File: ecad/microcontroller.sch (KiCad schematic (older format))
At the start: 2 parts, among them J4 Nucleo_F446_LHS, J5 Nucleo_F446_RHS

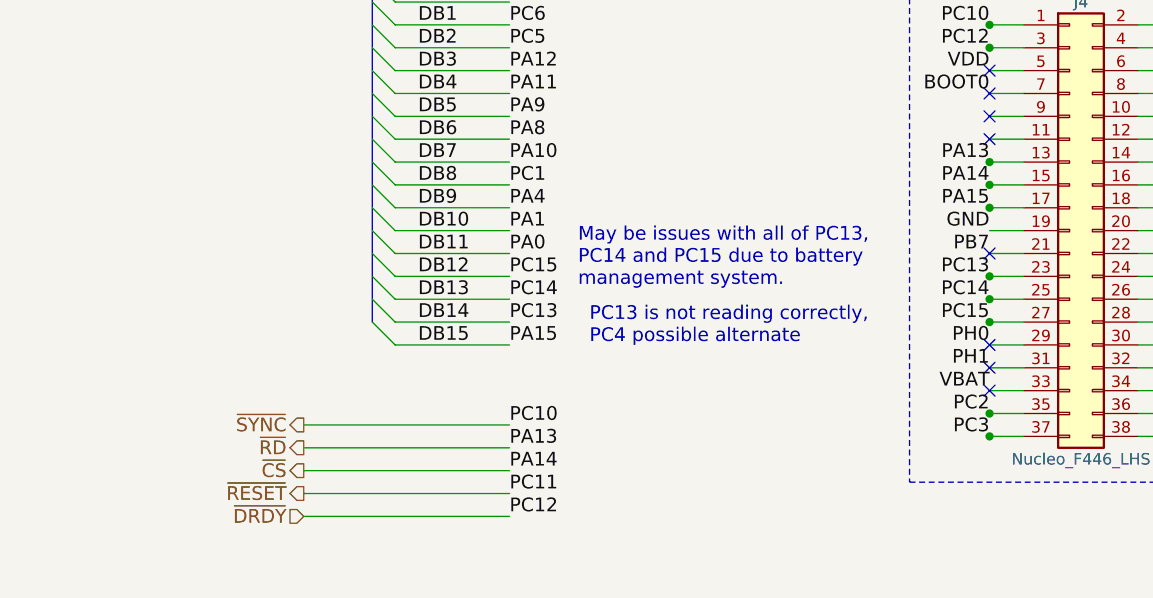
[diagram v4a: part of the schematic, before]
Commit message: Sort out all necessary pin changes.
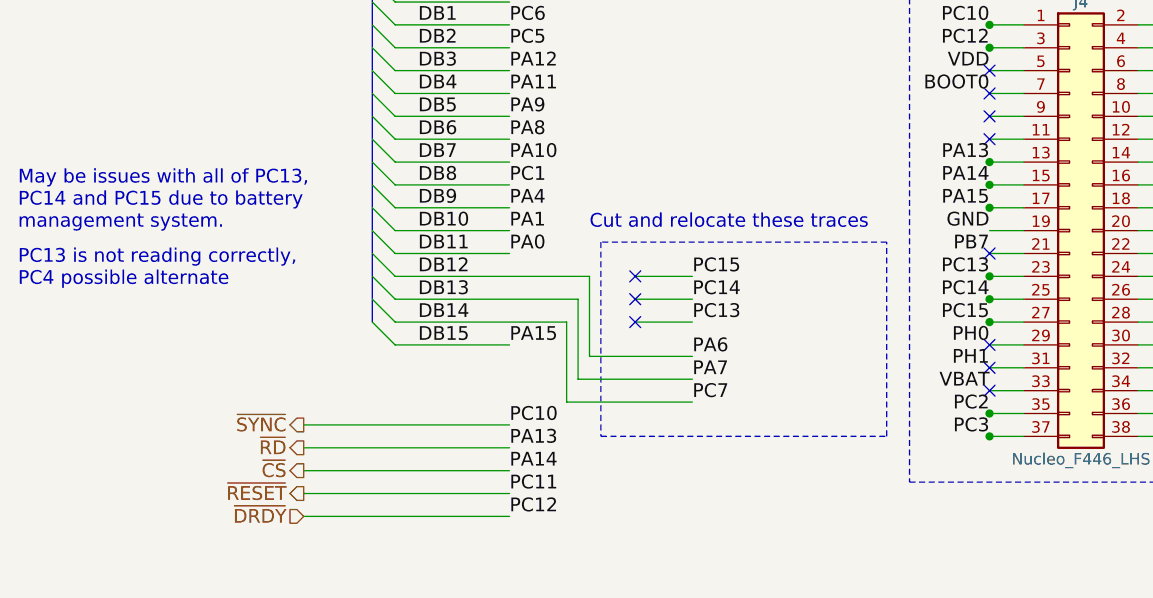
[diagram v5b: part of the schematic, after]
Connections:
- net PA6 is gone; now on net DB12: J5.13 (Pin_13)
- net PA7 is gone; now on net DB13: J5.15 (Pin_15)
- net PC7 is gone; now on net DB14: J5.19 (Pin_19)
- net DB12: no longer J4.27 (Pin_27)
- net DB13: no longer J4.25 (Pin_25)
- net DB14: no longer J4.23 (Pin_23)
- new net PC13: J4.23 (Pin_23)
- new net PC14: J4.25 (Pin_25)
- new net PC15: J4.27 (Pin_27)
- no-connect marks 48 -> 51
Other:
- note added: "Cut and relocate these traces"
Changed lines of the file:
@@
 Text Label 6150 3500 0    60   ~ 0
 PC12
-Text Label 6150 2650 0    60   ~ 0
+Text Label 6950 2650 0    60   ~ 0
 PC13
-Text Label 6150 2550 0    60   ~ 0
+Text Label 6950 2550 0    60   ~ 0
 PC14
-Text Label 6150 2450 0    60   ~ 0
+Text Label 6950 2450 0    60   ~ 0
 PC15
 Text Label 6150 3200 0    60   ~ 0
@@
 NoConn ~ 8250 2350
 NoConn ~ 8250 2950
+NoConn ~ 10250 4400
+NoConn ~ 10250 4500
+NoConn ~ 10250 4600
+NoConn ~ 10250 4700
+NoConn ~ 10250 4800
+NoConn ~ 10250 4900
+NoConn ~ 10250 5000
+NoConn ~ 10250 5100
+NoConn ~ 10250 5200
+NoConn ~ 10250 5300
+NoConn ~ 10250 5400
+NoConn ~ 10250 5500
+NoConn ~ 9800 1650
+$Comp
+L Conn_02x19_Odd_Even J4
+U 1 1 5ACD5E6B
+P 8600 2250
+F 0 "J4" H 8650 3250 50  0000 C CNN
+F 1 "Nucleo_F446_LHS" H 8650 1250 50  0000 C CNN
+F 2 "Pin_Headers:Pin_Header_Straight_2x19_Pitch2.54mm" H 8600 2250 50  0001 C CNN
+F 3 "" H 8600 2250 50  0001 C CNN
+	1    8600 2250
+	1    0    0    -1
+$EndComp
+$Comp
+L Conn_02x19_Odd_Even J5
+U 1 1 5ACD5EA9
+P 10150 2250
+F 0 "J5" H 10200 3250 50  0000 C CNN
+F 1 "Nucleo_F446_RHS" H 10200 1250 50  0000 C CNN
+F 2 "Pin_Headers:Pin_Header_Straight_2x19_Pitch2.54mm" H 10150 2250 50  0001 C CNN
+F 3 "" H 10150 2250 50  0001 C CNN
+	1    10150 2250
+	1    0    0    -1
+$EndComp
+Text Notes 4000 2500 0    60   ~ 0
+PC13 is not reading correctly, \nPC4 possible alternate
+Text Notes 4000 2250 0    60   ~ 0
+May be issues with all of PC13, \nPC14 and PC15 due to battery \nmanagement system.
+NoConn ~ 6700 2650
+Text Label 6950 3000 0    60   ~ 0
+PC7
+Text Notes 6500 2250 0    60   ~ 0
+Cut and relocate these traces
 Wire Wire Line
 	8250 1350 8400 1350
@@
 Wire Wire Line
 	5650 2350 6150 2350
-Wire Wire Line
-	5650 2450 6150 2450
-Wire Wire Line
-	5650 2550 6150 2550
-Wire Wire Line
-	5650 2650 6150 2650
 Wire Bus Line
 	5550 1150 5550 2650
@@
 Wire Notes Line
 	9750 5550 9750 4250
-NoConn ~ 10250 4400
-NoConn ~ 10250 4500
-NoConn ~ 10250 4600
-NoConn ~ 10250 4700
-NoConn ~ 10250 4800
-NoConn ~ 10250 4900
-NoConn ~ 10250 5000
-NoConn ~ 10250 5100
-NoConn ~ 10250 5200
-NoConn ~ 10250 5300
-NoConn ~ 10250 5400
-NoConn ~ 10250 5500
-NoConn ~ 9800 1650
 Wire Wire Line
 	5650 2750 6150 2750
-$Comp
-L Conn_02x19_Odd_Even J4
-U 1 1 5ACD5E6B
-P 8600 2250
-F 0 "J4" H 8650 3250 50  0000 C CNN
-F 1 "Nucleo_F446_LHS" H 8650 1250 50  0000 C CNN
-F 2 "Pin_Headers:Pin_Header_Straight_2x19_Pitch2.54mm" H 8600 2250 50  0001 C CNN
-F 3 "" H 8600 2250 50  0001 C CNN
-	1    8600 2250
-	1    0    0    -1
-$EndComp
-$Comp
-L Conn_02x19_Odd_Even J5
-U 1 1 5ACD5EA9
-P 10150 2250
-F 0 "J5" H 10200 3250 50  0000 C CNN
-F 1 "Nucleo_F446_RHS" H 10200 1250 50  0000 C CNN
-F 2 "Pin_Headers:Pin_Header_Straight_2x19_Pitch2.54mm" H 10150 2250 50  0001 C CNN
-F 3 "" H 10150 2250 50  0001 C CNN
-	1    10150 2250
-	1    0    0    -1
-$EndComp
-Text Notes 6500 2750 0    60   ~ 0
-PC13 is not reading correctly, \nPC4 possible alternate
-Text Notes 6450 2500 0    60   ~ 0
-May be issues with all of PC13, \nPC14 and PC15 due to battery \nmanagement system.
+Wire Wire Line
+	6950 2650 6700 2650
+Wire Wire Line
+	5650 2650 6400 2650
+Wire Wire Line
+	6400 2650 6400 3000
+Wire Wire Line
+	6400 3000 6950 3000
+NoConn ~ 6700 2550
+NoConn ~ 6700 2450
+Wire Wire Line
+	6700 2450 6950 2450
+Wire Wire Line
+	6700 2550 6950 2550
+Wire Wire Line
+	5650 2450 6500 2450
+Wire Wire Line
+	5650 2550 6450 2550
+Wire Wire Line
+	6450 2550 6450 2900
+Wire Wire Line
+	6450 2900 6950 2900
+Wire Wire Line
+	6500 2450 6500 2800
+Wire Wire Line
+	6500 2800 6950 2800
+Text Label 6950 2800 0    60   ~ 0
+PA6
+Text Label 6950 2900 0    60   ~ 0
+PA7
+Wire Notes Line
+	6550 2300 6550 3150
+Wire Notes Line
+	6550 3150 7800 3150
+Wire Notes Line
+	7800 3150 7800 2300
+Wire Notes Line
+	7800 2300 6550 2300
 $EndSCHEMATC
